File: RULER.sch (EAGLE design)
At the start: 0 parts

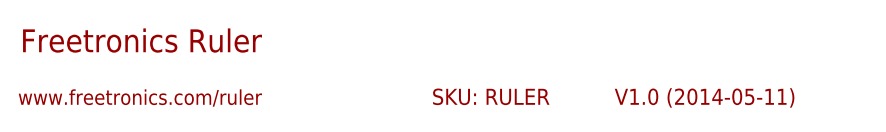
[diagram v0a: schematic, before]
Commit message: Changed silkscreen to fix URL
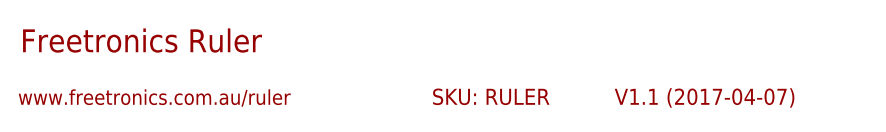
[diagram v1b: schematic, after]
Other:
- note added: "V1.1 (2017-04-07)"
- note added: "www.freetronics.com.au/ruler"
- note removed: "V1.0 (2014-05-11)"
- note removed: "www.freetronics.com/ruler"
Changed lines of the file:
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@@
 <plain>
 <text x="149.86" y="12.7" size="2.54" layer="94">Freetronics Ruler</text>
-<text x="215.9" y="6.858" size="1.778" layer="94">V1.0 (2014-05-11)</text>
-<text x="149.606" y="6.858" size="1.651" layer="94">www.freetronics.com/ruler</text>
+<text x="215.9" y="6.858" size="1.778" layer="94">V1.1 (2017-04-07)</text>
+<text x="149.606" y="6.858" size="1.651" layer="94">www.freetronics.com.au/ruler</text>
 <text x="195.58" y="6.858" size="1.778" layer="94">SKU: RULER</text>
 <frame x1="0" y1="0" x2="248.92" y2="185.42" columns="8" rows="5" layer="94"/>
